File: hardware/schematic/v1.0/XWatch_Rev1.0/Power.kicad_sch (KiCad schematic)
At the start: 3 parts, among them CN1 FH19C-8S-0.5SH, CN2 504208-2410, IC3 SGM38046YG_TR

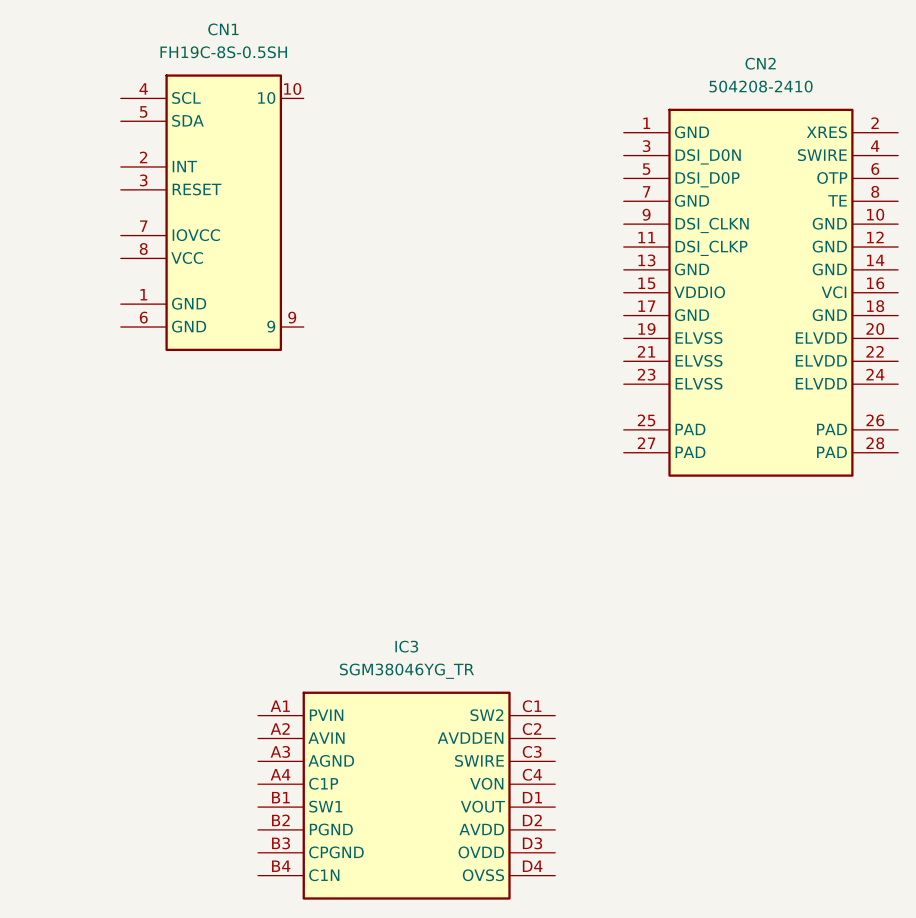
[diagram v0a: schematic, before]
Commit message: Add schematic sub-sheets and component libraries for Rev1.0
- Add Power, GNSS, Sensors, Memory and Connectivity schematic sheets
- Add symbols/footprints for DA9168, SGM38046, MAX86141, BMI270, LSM6DSOX, LIS2MDL, AK09918C, NT3H1101
- Add 3D models for new parts
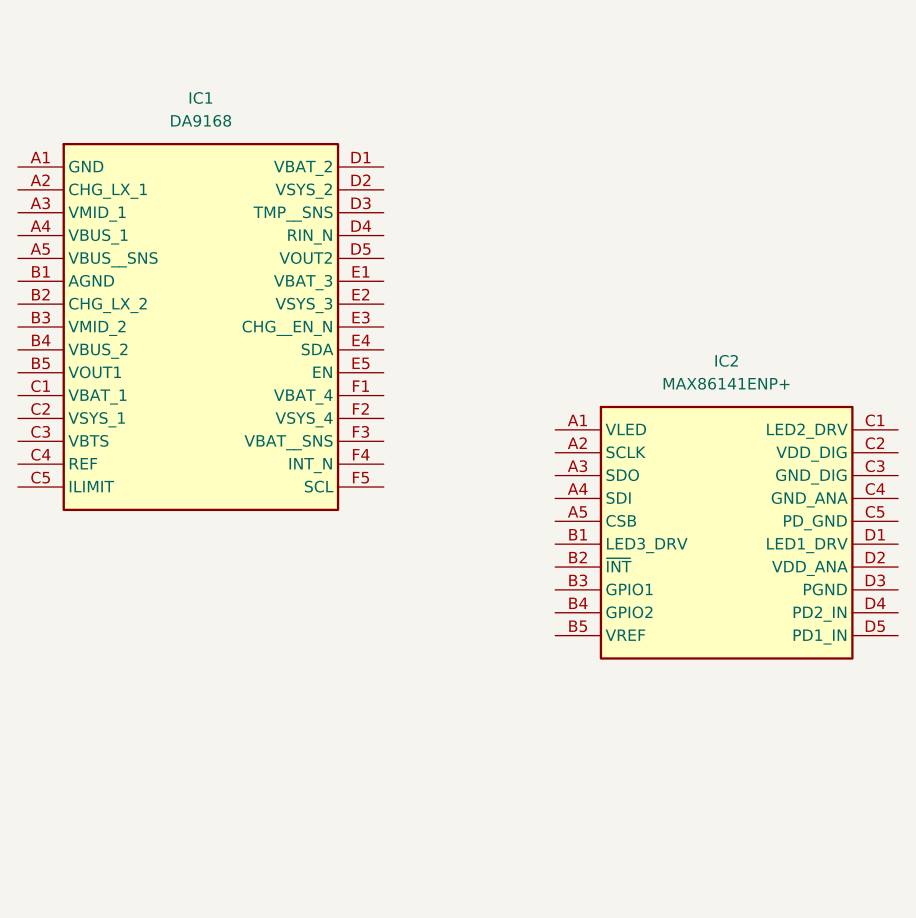
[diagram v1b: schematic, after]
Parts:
- removed CN1: FH19C-8S-0.5SH, XWatch_Rev1.0:FH19C-8S-0_5SH_10, symbol XWatch_Rev1.0:FH19C-8S-0.5SH
- removed CN2: 504208-2410, XWatch_Rev1.0:5042082410, symbol XWatch_Rev1.0:504208-2410
- removed IC3: SGM38046YG_TR, XWatch_Rev1.0:BGA16C50P4X4_200X200X61, symbol XWatch_Rev1.0:SGM38046YG_TR
- added IC1: DA9168, XWatch_Rev1.0:BGA30C40P5X6_214X254X56, symbol XWatch_Rev1.0:DA9168
- added IC2: MAX86141ENP+, XWatch_Rev1.0:BGA20C40P5X4_205X185X50, symbol XWatch_Rev1.0:MAX86141ENP+

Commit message: doc and sch update
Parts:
- removed IC2: MAX86141ENP+, XWatch_Rev1.0:BGA20C40P5X4_205X185X50, symbol XWatch_Rev1.0:MAX86141ENP+
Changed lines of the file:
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@@
-		)
-	)
-	(symbol
-		(lib_id "XWatch_Rev1.0:MAX86141ENP+")
-		(at 140.97 109.22 0)
-		(unit 1)
-		(body_style 1)
-		(exclude_from_sim no)
-		(in_bom yes)
-		(on_board yes)
-		(in_pos_files yes)
-		(dnp no)
-		(fields_autoplaced yes)
-		(property "Reference" "IC2"
-			(at 140.97 92.71 0)
-			(show_name no)
-			(do_not_autoplace no)
-			(effects
-				(font
-					(size 1.27 1.27)
-				)
-			)
-		)
-		(property "Value" "MAX86141ENP+"
-			(at 140.97 95.25 0)
-			(show_name no)
-			(do_not_autoplace no)
-			(effects
-				(font
-					(size 1.27 1.27)
-				)
-			)
-		)
-		(property "Footprint" "XWatch_Rev1.0:BGA20C40P5X4_205X185X50"
-			(at 175.26 204.14 0)
-			(hide yes)
-			(show_name no)
-			(do_not_autoplace no)
-			(effects
-				(font
-					(size 1.27 1.27)
-				)
-				(justify left top)
-			)
-		)
-		(property "Datasheet" "https://datasheets.maximintegrated.com/en/ds/MAX86140-MAX86141.pdf"
-			(at 175.26 304.14 0)
-			(hide yes)
-			(show_name no)
-			(do_not_autoplace no)
-			(effects
-				(font
-					(size 1.27 1.27)
-				)
-				(justify left top)
-			)
-		)
-		(property "Description" "MAXIM INTEGRATED PRODUCTS - MAX86141ENP+ - PULSE OXIMETER/HEART RATE SENSOR, WLP-20"
-			(at 140.97 109.22 0)
-			(hide yes)
-			(show_name no)
-			(do_not_autoplace no)
-			(effects
-				(font
-					(size 1.27 1.27)
-				)
-			)
-		)
-		(property "Height" "0.5"
-			(at 175.26 504.14 0)
-			(hide yes)
-			(show_name no)
-			(do_not_autoplace no)
-			(effects
-				(font
-					(size 1.27 1.27)
-				)
-				(justify left top)
-			)
-		)
-		(property "Manufacturer_Name" "Analog Devices"
-			(at 175.26 604.14 0)
-			(hide yes)
-			(show_name no)
-			(do_not_autoplace no)
-			(effects
-				(font
-					(size 1.27 1.27)
-				)
-				(justify left top)
-			)
-		)
-		(property "Manufacturer_Part_Number" "MAX86141ENP+"
-			(at 175.26 704.14 0)
-			(hide yes)
-			(show_name no)
-			(do_not_autoplace no)
-			(effects
-				(font
-					(size 1.27 1.27)
-				)
-				(justify left top)
-			)
-		)
-		(property "Mouser Part Number" "700-MAX86141ENP+"
-			(at 175.26 804.14 0)
-			(hide yes)
-			(show_name no)
-			(do_not_autoplace no)
-			(effects
-				(font
-					(size 1.27 1.27)
-				)
-				(justify left top)
-			)
-		)
-		(property "Mouser Price/Stock" "https://www.mouser.co.uk/ProductDetail/Analog-Devices-Maxim-Integrated/MAX86141ENP%2b?qs=YCa%2FAAYMW01jqVI3kzZSjA%3D%3D"
-			(at 175.26 904.14 0)
-			(hide yes)
-			(show_name no)
-			(do_not_autoplace no)
-			(effects
-				(font
-					(size 1.27 1.27)
-				)
-				(justify left top)
-			)
-		)
-		(property "Arrow Part Number" ""
-			(at 175.26 1004.14 0)
-			(hide yes)
-			(show_name no)
-			(do_not_autoplace no)
-			(effects
-				(font
-					(size 1.27 1.27)
-				)
-				(justify left top)
-			)
-		)
-		(property "Arrow Price/Stock" ""
-			(at 175.26 1104.14 0)
-			(hide yes)
-			(show_name no)
-			(do_not_autoplace no)
-			(effects
-				(font
-					(size 1.27 1.27)
-				)
-				(justify left top)
-			)
-		)
-		(pin "C2"
-		)
-		(pin "C3"
-		)
-		(pin "D3"
-		)
-		(pin "A1"
-		)
-		(pin "D4"
-		)
-		(pin "D1"
-		)
-		(pin "B3"
-		)
-		(pin "B5"
-		)
-		(pin "A4"
-		)
-		(pin "A5"
-		)
-		(pin "D5"
-		)
-		(pin "A2"
-		)
-		(pin "C5"
-		)
-		(pin "B4"
-		)
-		(pin "B2"
-		)
-		(pin "D2"
-		)
-		(pin "B1"
-		)
-		(pin "C4"
-		)
-		(pin "A3"
-		)
-		(pin "C1"
-		)
-		(instances
-			(project "XWatch_Rev1.0"
-				(path "/2e5e9480-7d2e-4148-a9bf-0ac7d46b20bc/c1d925a8-200b-4a74-8f49-eb244dc4dc34"
-					(reference "IC2")
-					(unit 1)
-				)
-			)
 		)
 	)

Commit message: sch and doc update
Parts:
- added U4: MAX17048G_T10, XWatch_Rev1.0:MAX17048G_T10, symbol XWatch_Rev1.0:MAX17048G_T10
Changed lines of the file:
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@@
+		)
+	)
+	(symbol
+		(lib_id "XWatch_Rev1.0:MAX17048G_T10")
+		(at 168.91 110.49 0)
+		(unit 1)
+		(body_style 1)
+		(exclude_from_sim no)
+		(in_bom yes)
+		(on_board yes)
+		(in_pos_files yes)
+		(dnp no)
+		(fields_autoplaced yes)
+		(property "Reference" "U4"
+			(at 168.91 97.79 0)
+			(show_name no)
+			(do_not_autoplace no)
+			(effects
+				(font
+					(size 1.27 1.27)
+				)
+			)
+		)
+		(property "Value" "MAX17048G_T10"
+			(at 168.91 100.33 0)
+			(show_name no)
+			(do_not_autoplace no)
+			(effects
+				(font
+					(size 1.27 1.27)
+				)
+			)
+		)
+		(property "Footprint" "XWatch_Rev1.0:MAX17048G_T10"
+			(at 168.91 110.49 0)
+			(hide yes)
+			(show_name no)
+			(do_not_autoplace no)
+			(effects
+				(font
+					(size 1.27 1.27)
+				)
+			)
+		)
+		(property "Datasheet" "https://www.lcsc.com/datasheet/lcsc_datasheet_2410121738_Analog-Devices-Inc--Maxim-Integrated-MAX17048G-T10_C2682616.pdf"
+			(at 168.91 110.49 0)
+			(hide yes)
+			(show_name no)
+			(do_not_autoplace no)
+			(effects
+				(font
+					(size 1.27 1.27)
+				)
+			)
+		)
+		(property "Description" "-40℃~+85℃ 1 2.5V~4.5V 3uA I2C Lithium Battery Not supported Not supported DFN-8-EP(2x2) Battery Management ROHS"
+			(at 168.91 110.49 0)
+			(hide yes)
+			(show_name no)
+			(do_not_autoplace no)
+			(effects
+				(font
+					(size 1.27 1.27)
+				)
+			)
+		)
+		(property "LCSC" "C2682616"
+			(at 168.91 110.49 0)
+			(hide yes)
+			(show_name no)
+			(do_not_autoplace no)
+			(effects
+				(font
+					(size 1.27 1.27)
+				)
+			)
+		)
+		(property "Manufacturer" "Analog Devices Inc./Maxim Integrated"
+			(at 168.91 110.49 0)
+			(hide yes)
+			(show_name no)
+			(do_not_autoplace no)
+			(effects
+				(font
+					(size 1.27 1.27)
+				)
+			)
+		)
+		(property "Manufacturer Part" "MAX17048G+T10"
+			(at 168.91 110.49 0)
+			(hide yes)
+			(show_name no)
+			(do_not_autoplace no)
+			(effects
+				(font
+					(size 1.27 1.27)
+				)
+			)
+		)
+		(pin "1"
+		)
+		(pin "3"
+		)
+		(pin "8"
+		)
+		(pin "9"
+		)
+		(pin "5"
+		)
+		(pin "7"
+		)
+		(pin "2"
+		)
+		(pin "6"
+		)
+		(pin "4"
+		)
+		(instances
+			(project "XWatch_Rev1.0"
+				(path "/2e5e9480-7d2e-4148-a9bf-0ac7d46b20bc/c1d925a8-200b-4a74-8f49-eb244dc4dc34"
+					(reference "U4")
+					(unit 1)
+				)
+			)
 		)
 	)

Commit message: sch update
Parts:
- removed IC1: DA9168, XWatch_Rev1.0:BGA30C40P5X6_214X254X56, symbol XWatch_Rev1.0:DA9168
- added C31: 47nF, XWatch_Rev1.0:GEN_C_0201, symbol XWatch_Rev1.0:C
- added C32, C33, C34, C35: 10uF, XWatch_Rev1.0:GEN_C_0402, symbol XWatch_Rev1.0:C
- added C36, C37: 1uF, XWatch_Rev1.0:GEN_C_0402, symbol XWatch_Rev1.0:C
- added C38: 100nF, XWatch_Rev1.0:GEN_C_0201, symbol XWatch_Rev1.0:C
- added C39: 2.2uF, XWatch_Rev1.0:GEN_C_0402, symbol XWatch_Rev1.0:C
- added L2: 2.2uH, XWatch_Rev1.0:L_0402_1005Metric, symbol XWatch_Rev1.0:L
- added U10: DA9168, symbol XWatch_Rev1.0:DA9168_1
- added U9: TPS62840DLCR, XWatch_Rev1.0:TPS62840DLCR, symbol XWatch_Rev1.0:TPS62840DLCR
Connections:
- new net: C31.1, L2.1, U10.A2,B2 (CHG_LX)
- new net: C31.2, U10.C3 (VBTS)
- new net: C32.1, C33.1, U10.A3,B3 (VMID)
- new net GND: C32.2, C33.2, C34.2, C35.2, C36.2, C37.2, C38.2, C39.2, U10.A1 (GND), U10.B1 (AGND)
- new net PMIC_CHG_EN_N: U10.E3 (CHG__EN_N)
- new net PMIC_EN: U10.E5 (EN)
- new net PMIC_INT_N: U10.F4 (INT_N)
- new net PMIC_RIN_N: U10.D4 (RIN_N)
- new net PMIC_SCL: U10.F5 (SCL)
- new net PMIC_SDA: U10.E4 (SDA)
- new net VBAT: C38.1, C39.1, U10.C1,D1,E1,F1 (VBAT), U10.F3 (VBAT__SNS)
- new net VBUS: C36.1, C37.1, U10.A4,B4 (VBUS), U10.A5 (VBUS__SNS)
- new net VSYS: C34.1, C35.1, L2.2, U10.C2,D2,E2,F2 (VSYS)
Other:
- moved on the sheet: U4
